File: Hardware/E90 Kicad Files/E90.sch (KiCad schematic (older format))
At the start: 108 parts, among them J1 Conn_01x03, J10 SJ-63073E, J2 SWD Connector Conn_02x03, J3 Power Test Point Conn_01x02, J4 Conn_01x03, J5 Conn_01x02, J6 Conn_01x03, J7 USB_B_Mini, J8 Barrel_Jack_Switch, J9 SJ-63073E, U1 AMS1117-3.3, U2 CS4344_CZZ, U3 TLV2774, U4 CS5343_CZZ, U5 STM32F407VGT60, U6 USBLC6-2SC6

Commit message: iir
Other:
- moved on the sheet: ADC1_IN1, ADC1_IN2, ADC1_IN3, C1, C13, C14, C15, C16, C17, C18, C19, C2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

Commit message: fixed pot orientation
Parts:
- removed C10, C35, C9: 10uF, Capacitor_SMD:C_0603_1608Metric, symbol Device:C_Small
- removed C12: 2.7nF, Capacitor_SMD:C_0603_1608Metric, symbol Device:C_Small
- removed C23, C3, C33, C8: 100nf, Capacitor_SMD:C_0402_1005Metric, symbol Device:C_Small
- removed C24, C4: 4.7uF, Capacitor_SMD:C_0603_1608Metric, symbol Device:C_Small
- removed C25, C5: 100nF, Capacitor_SMD:C_0402_1005Metric, symbol Device:C_Small
- removed C32, C34: 1uF, Capacitor_SMD:C_0603_1608Metric, symbol Device:C_Small
- removed C36: 180pF, Capacitor_SMD:C_0603_1608Metric, symbol Device:C_Small
- removed C7: 3.3uF, Capacitor_SMD:C_0603_1608Metric, symbol Device:C_Small
- removed FB2, FB4: 600 @100 MHz, Inductor_SMD:L_0805_2012Metric, symbol Device:Ferrite_Bead_Small
- removed R10: 10k, Resistor_SMD:R_0603_1608Metric, symbol Device:R_Small_US
- removed R11, R13: 5.1K, Resistor_SMD:R_0603_1608Metric, symbol Device:R_Small_US
- removed R2, R7: 1, Resistor_SMD:R_0805_2012Metric, symbol Device:R_Small_US
- removed R4: 470, Resistor_SMD:R_0603_1608Metric, symbol Device:R_Small_US
- removed R6: 10K, Resistor_SMD:R_0603_1608Metric, symbol Device:R_Small_US
- removed U2: CS4344_CZZ, Package_TSSOP_SMD:SOP50P490X110-10N, symbol E90_Embedded_DSP:CS4344_CZZ
- removed U4: CS5343_CZZ, Package_TSSOP_SMD:SOP50P490X110-10N, symbol E90_Embedded_DSP:CS5343_CZZ
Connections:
- net +3V3: now also ADC1_IN1.1, ADC1_IN2.1, ADC1_IN3.1; no longer ADC1_IN1.3, ADC1_IN2.3, ADC1_IN3.3
- net GND: now also ADC1_IN1.3, ADC1_IN2.3, ADC1_IN3.3; no longer ADC1_IN1.1, ADC1_IN2.1, ADC1_IN3.1
- no-connect marks 64 -> 62
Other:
- note removed: "A/D\n"
- note removed: "D/A"
- moved on the sheet: ADC1_IN1, ADC1_IN2, ADC1_IN3, C11, C13, C14, C15, C16, C17, C18, C19, C20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

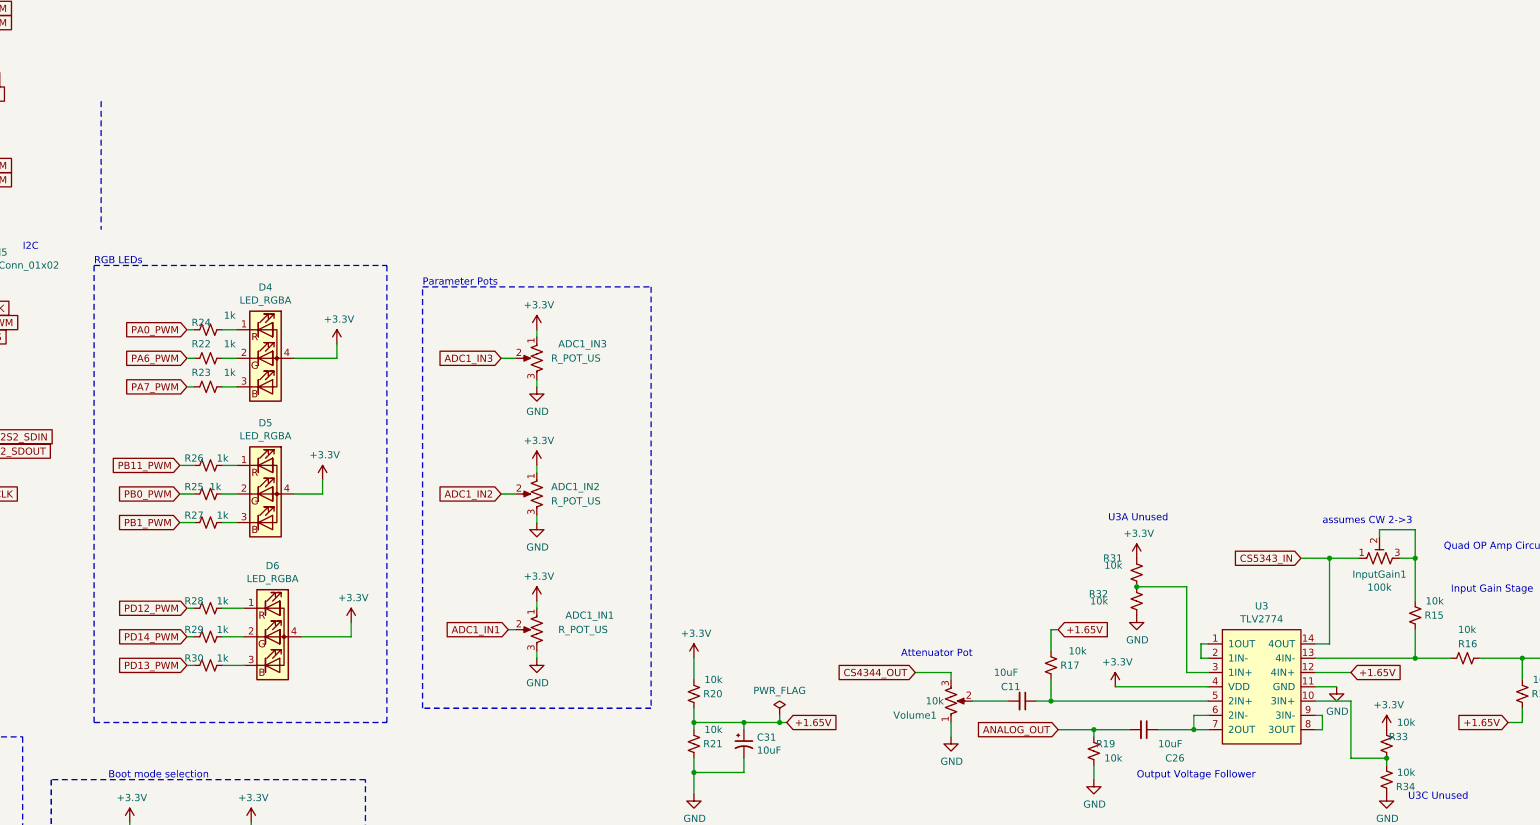
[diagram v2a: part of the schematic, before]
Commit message: fixed pot orientation
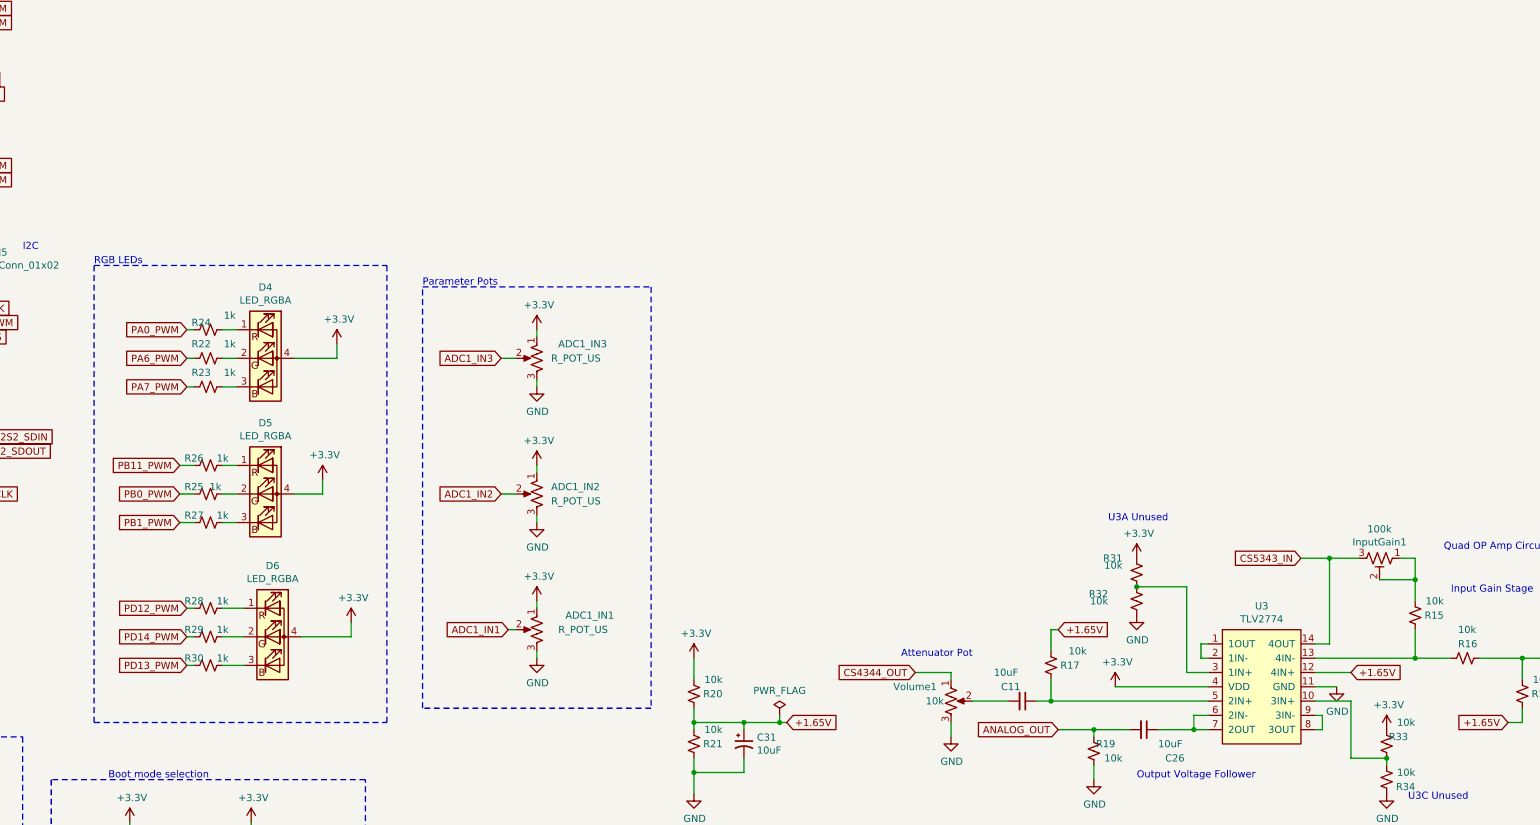
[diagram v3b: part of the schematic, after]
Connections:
- net CS4344_OUT: now also Volume1.1; no longer Volume1.3
- net CS5343_IN: now also InputGain1.3; no longer InputGain1.1
- net GND: now also Volume1.3; no longer Volume1.1
- net at InputGain1.2, R15.1: now also InputGain1.1; no longer InputGain1.3
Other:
- note removed: "assumes CW 2->3\n\n"
- moved on the sheet: InputGain1
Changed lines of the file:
@@
 F 3 "~" H 11350 14200 50  0001 C CNN
 	1    11350 14200
-	1    0    0    1
+	1    0    0    -1
 $EndComp
 $Comp
@@
 	14500 13200 14600 13200
 Wire Wire Line
-	14600 13200 14600 13500
+	14600 13200 14600 13350
 Wire Wire Line
 	10150 14300 10150 14350
@@
 	1    0    0    -1
 $EndComp
-Wire Notes Line
-	5400 10000 5400 10900
 $Comp
 L power:+5V #PWR048
@@
 Wire Wire Line
 	7600 1500 7600 1550
-Connection ~ 14600 13200
-Wire Wire Line
-	14350 13050 14350 13000
-Wire Wire Line
-	14600 13000 14600 13200
-Wire Wire Line
-	14350 13000 14600 13000
 Text Notes 12450 12950 0    50   ~ 0
 U3A Unused
@@
 F 3 "~" H 14350 13200 50  0001 C CNN
 	1    14350 13200
-	0    -1   -1   0
-$EndComp
-Text Notes 13950 13050 0    50   ~ 0
-assumes CW 2->3\n\n
+	0    1    1    0
+$EndComp
 Wire Notes Line
 	5350 11150 7400 11150
@@
 	-1   0    0    1
 $EndComp
+Wire Wire Line
+	14350 13350 14600 13350
+Connection ~ 14600 13350
+Wire Wire Line
+	14600 13350 14600 13500
 $EndSCHEMATC

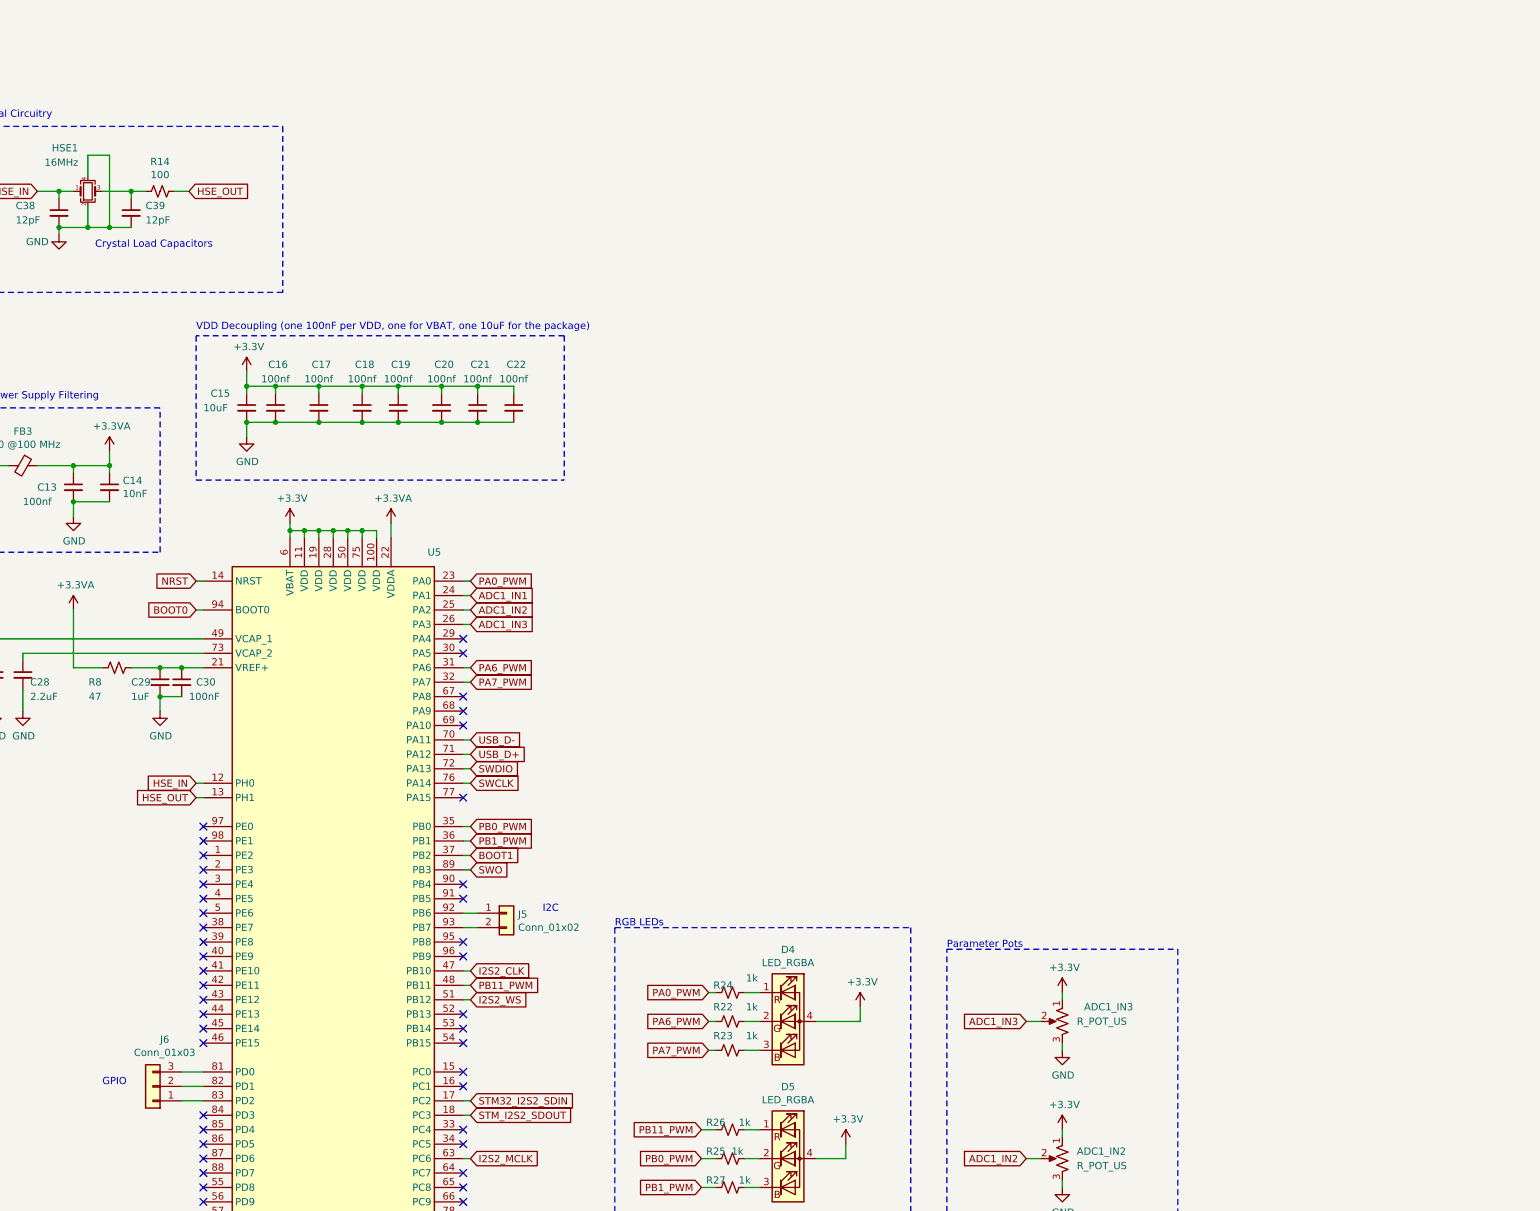
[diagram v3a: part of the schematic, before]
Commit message: added WM8731 codec part to schem
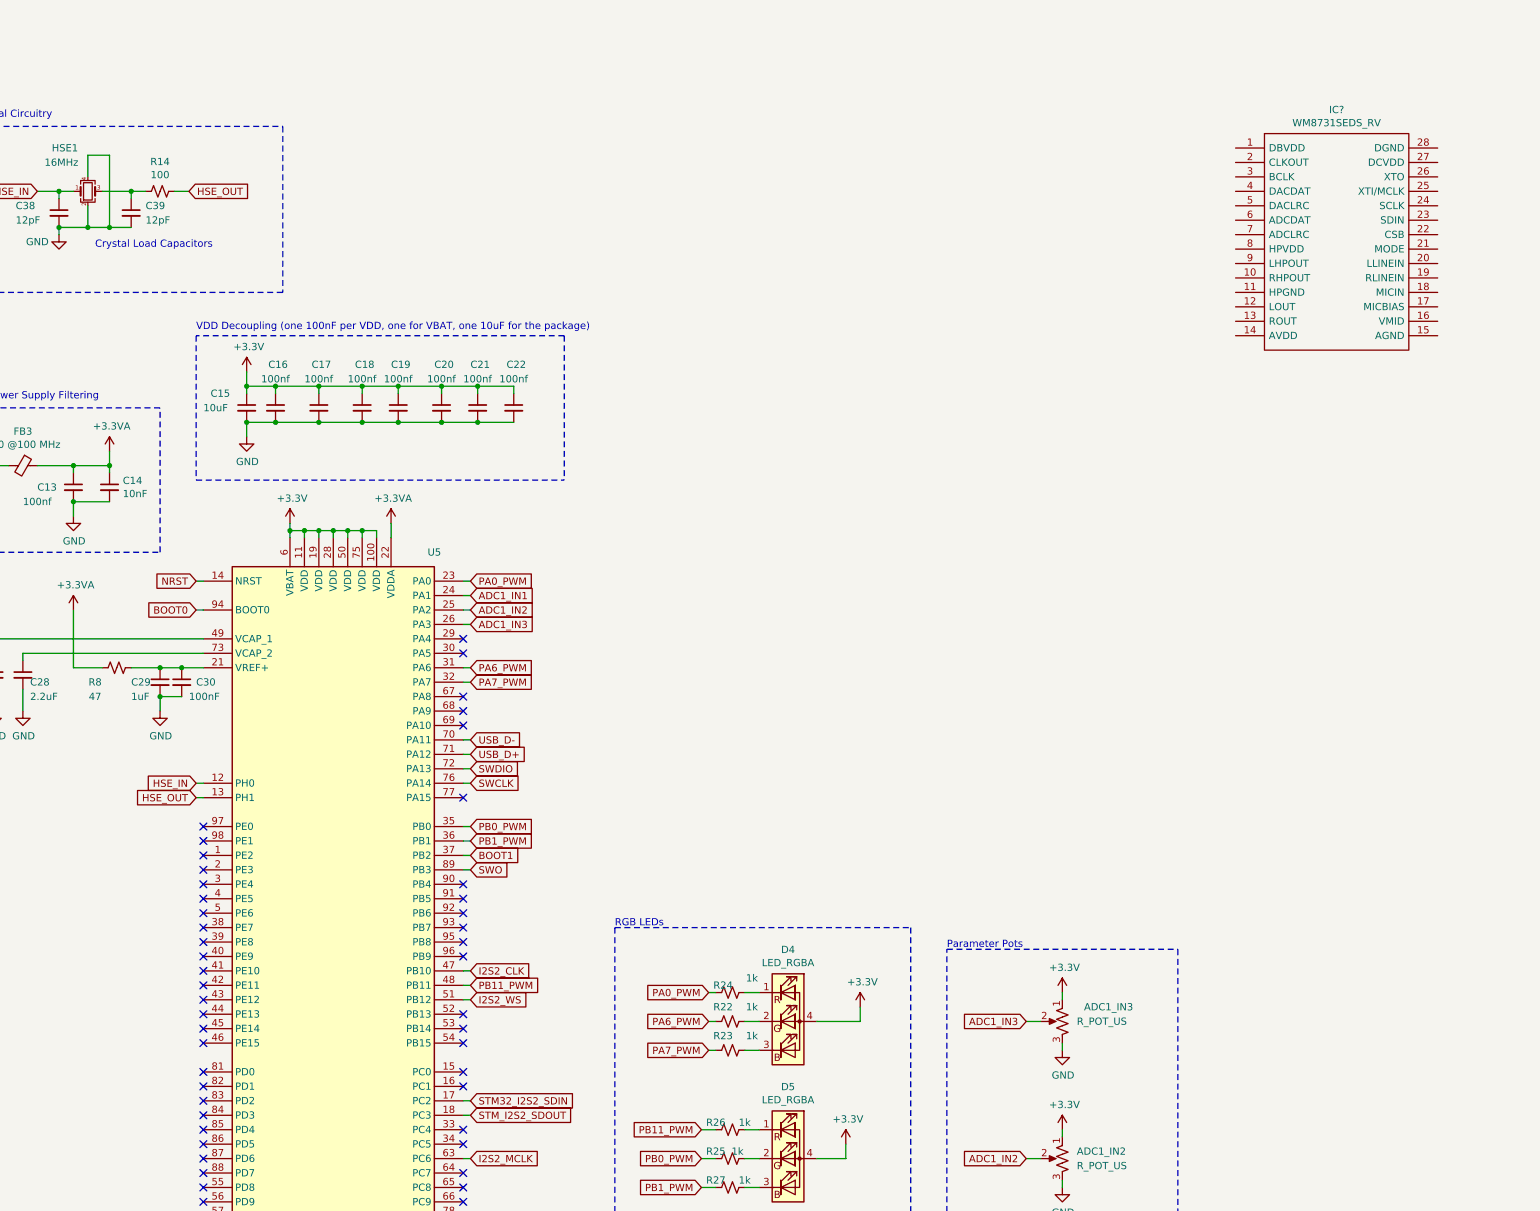
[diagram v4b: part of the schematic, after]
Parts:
- removed J5: Conn_01x02, Connector_PinHeader_2.54mm:PinHeader_1x02_P2.54mm_Vertical, symbol Connector_Generic:Conn_01x02
- removed J6: Conn_01x03, Connector_PinHeader_2.54mm:PinHeader_1x03_P2.54mm_Vertical, symbol Connector_Generic:Conn_01x03
- added IC?: WM8731SEDS_RV, SOP65P780X200-28N, symbol E90_Embedded_DSP:WM8731SEDS_RV
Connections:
- no-connect marks 62 -> 67
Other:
- note removed: "GPIO"
- note removed: "I2C"
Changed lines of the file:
@@
 	1550 15350 1500 15350
-Wire Wire Line
-	2500 12150 2350 12150
-Wire Wire Line
-	2500 12350 2350 12350
-$Comp
-L Connector_Generic:Conn_01x03 J6
-U 1 1 61089AAA
-P 2150 12250
-F 0 "J6" H 2068 11925 50  0000 C CNN
-F 1 "Conn_01x03" H 2068 12016 50  0000 C CNN
-F 2 "Connector_PinHeader_2.54mm:PinHeader_1x03_P2.54mm_Vertical" H 2150 12250 50  0001 C CNN
-F 3 "~" H 2150 12250 50  0001 C CNN
-	1    2150 12250
-	-1   0    0    1
-$EndComp
-Wire Wire Line
-	2500 12250 2350 12250
-Text Notes 1800 12250 0    50   ~ 0
-GPIO
-$Comp
-L Connector_Generic:Conn_01x02 J5
-U 1 1 610A99ED
-P 4600 11050
-F 0 "J5" H 4680 11042 50  0000 L CNN
-F 1 "Conn_01x02" H 4680 10951 50  0000 L CNN
-F 2 "Connector_PinHeader_2.54mm:PinHeader_1x02_P2.54mm_Vertical" H 4600 11050 50  0001 C CNN
-F 3 "~" H 4600 11050 50  0001 C CNN
-	1    4600 11050
-	1    0    0    -1
-$EndComp
-Wire Wire Line
-	4400 11050 4300 11050
-Wire Wire Line
-	4400 11150 4300 11150
-Text Notes 4850 11050 0    50   ~ 0
-I2C
 Wire Wire Line
 	15900 13900 15750 13900
@@
 Wire Wire Line
 	14600 13350 14600 13500
+NoConn ~ 4300 11050
+NoConn ~ 4300 11150
+NoConn ~ 2500 12150
+NoConn ~ 2500 12250
+NoConn ~ 2500 12350
+$Comp
+L E90_Embedded_DSP:WM8731SEDS_RV IC?
+U 1 1 62D482B7
+P 9650 5750
+F 0 "IC?" H 10350 6015 50  0000 C CNN
+F 1 "WM8731SEDS_RV" H 10350 5924 50  0000 C CNN
+F 2 "SOP65P780X200-28N" H 10900 5850 50  0001 L CNN
+F 3 "https://d3uzseaevmutz1.cloudfront.net/pubs/proDatasheet/WM8731_v4.9.pdf" H 10900 5750 50  0001 L CNN
+F 4 "WOLFSON MICROELECTRONICS - WM8731SEDS/RV - DAC, AUDIO, 24BIT, HEADPHONE, 28SSOP" H 10900 5650 50  0001 L CNN "Description"
+F 5 "2" H 10900 5550 50  0001 L CNN "Height"
+F 6 "WOLFSON MICROELECTRONICS" H 10900 5450 50  0001 L CNN "Manufacturer_Name"
+F 7 "WM8731SEDS/RV" H 10900 5350 50  0001 L CNN "Manufacturer_Part_Number"
+F 8 "" H 10900 5250 50  0001 L CNN "Mouser Part Number"
+F 9 "" H 10900 5150 50  0001 L CNN "Mouser Price/Stock"
+F 10 "" H 10900 5050 50  0001 L CNN "Arrow Part Number"
+F 11 "" H 10900 4950 50  0001 L CNN "Arrow Price/Stock"
+	1    9650 5750
+	1    0    0    -1
+$EndComp
 $EndSCHEMATC

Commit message: schem
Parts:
- added C? (x3): 100nf, Capacitor_SMD:C_0402_1005Metric, symbol Device:C_Small
- added C? (x4): 10uF, Capacitor_SMD:C_0805_2012Metric, symbol Device:CP1_Small
- added C? (x3): 220pF, Capacitor_SMD:C_0402_1005Metric, symbol Device:C_Small
- added C? (x3): 1uF, Capacitor_SMD:C_0805_2012Metric, symbol Device:CP1_Small
- added C?: 100nF, Capacitor_SMD:C_0402_1005Metric, symbol Device:C_Small
- added R? (x2): 5.6k, Resistor_SMD:R_0603_1608Metric, symbol Device:R_Small_US
- added R?: 47k, Resistor_SMD:R_0603_1608Metric, symbol Device:R_Small_US
- added R?: 100, Resistor_SMD:R_0603_1608Metric, symbol Device:R_Small_US
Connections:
- net +3V3: now also IC?.1 (DBVDD), IC?.14 (AVDD), IC?.27 (DCVDD), IC?.8 (HPVDD), C?.1, C?.1, C?.1, C?.1, C?.1, C?.1, C?.1, C?.1
- net ANALOG_OUT: now also R?.1
- net GND: now also IC?.11 (HPGND), IC?.15 (AGND), IC?.18 (MICIN), IC?.19 (RLINEIN), IC?.28 (DGND), C?.1, C?.1, C?.1, C?.2, C?.2, C?.2, C?.2, C?.2, C?.2, C?.2, C?.2, C?.2, R?.1
- net I2S2_CLK: now also IC?.3 (BCLK)
- net I2S2_MCLK: now also IC?.25 (XTI/MCLK)
- net I2S2_WS: now also IC?.5 (DACLRC), IC?.7 (ADCLRC)
- net STM32_I2S2_SDIN: now also IC?.6 (ADCDAT)
- net STM_I2S2_SDOUT: now also IC?.4 (DACDAT)
- net at IC?.12 (LOUT): now also C?.1
- net at IC?.16 (VMID): now also C?.1, C?.2, C?.2
- net at IC?.20 (LLINEIN): now also C?.1
- net CS5343_IN renamed LINE_IN
- net LINE_IN: now also R?.1
- new net: C?.2, C?.2, R?.2, R?.2
- new net: C?.2, R?.2, R?.2
- no-connect marks 67 -> 72
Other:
- moved on the sheet: IC?
